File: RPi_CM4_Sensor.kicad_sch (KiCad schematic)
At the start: 16 parts, among them J1 RPi_pin, U1 SHT35, U2 SGP40, U3 APDS-9250, U4 SCD40

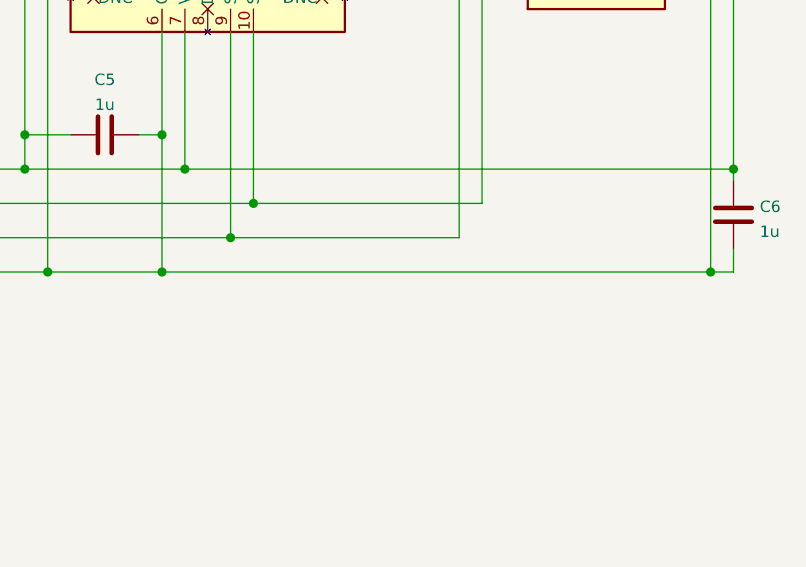
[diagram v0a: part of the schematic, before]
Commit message: feat: 温度センサを別基板に配置するためのピンヘッダを追加
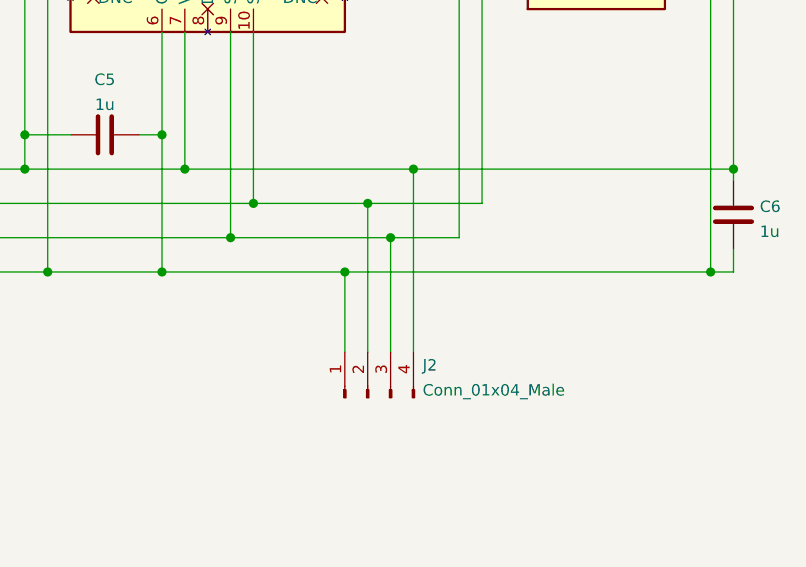
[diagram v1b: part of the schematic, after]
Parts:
- added J2: Conn_01x04_Male, Connector_PinHeader_2.54mm:PinHeader_1x04_P2.54mm_Vertical, symbol Connector:Conn_01x04_Male
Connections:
- net +3V3: now also J2.4 (Pin_4)
- net GND: now also J2.1 (Pin_1)
- net PIN_03: now also J2.2 (Pin_2)
- net PIN_05: now also J2.3 (Pin_3)
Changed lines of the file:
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@@
   (junction (at 209.55 88.9) (diameter 1.016) (color 0 0 0 0))
   (junction (at 212.09 85.09) (diameter 1.016) (color 0 0 0 0))
+  (junction (at 222.25 92.71) (diameter 1.016) (color 0 0 0 0))
+  (junction (at 224.79 85.09) (diameter 1.016) (color 0 0 0 0))
+  (junction (at 227.33 88.9) (diameter 1.016) (color 0 0 0 0))
+  (junction (at 229.87 81.28) (diameter 1.016) (color 0 0 0 0))
   (junction (at 262.89 92.71) (diameter 1.016) (color 0 0 0 0))
   (junction (at 265.43 81.28) (diameter 1.016) (color 0 0 0 0))
@@
     (stroke (width 0) (type solid) (color 0 0 0 0))
   )
-  (wire (pts (xy 201.93 92.71) (xy 262.89 92.71))
+  (wire (pts (xy 201.93 92.71) (xy 222.25 92.71))
     (stroke (width 0) (type solid) (color 0 0 0 0))
   )
@@
     (stroke (width 0) (type solid) (color 0 0 0 0))
   )
-  (wire (pts (xy 204.47 81.28) (xy 265.43 81.28))
+  (wire (pts (xy 204.47 81.28) (xy 229.87 81.28))
     (stroke (width 0) (type solid) (color 0 0 0 0))
   )
@@
     (stroke (width 0) (type solid) (color 0 0 0 0))
   )
-  (wire (pts (xy 209.55 88.9) (xy 234.95 88.9))
+  (wire (pts (xy 209.55 88.9) (xy 227.33 88.9))
     (stroke (width 0) (type solid) (color 0 0 0 0))
   )
@@
     (stroke (width 0) (type solid) (color 0 0 0 0))
   )
-  (wire (pts (xy 212.09 85.09) (xy 237.49 85.09))
+  (wire (pts (xy 212.09 85.09) (xy 224.79 85.09))
+    (stroke (width 0) (type solid) (color 0 0 0 0))
+  )
+  (wire (pts (xy 222.25 92.71) (xy 222.25 101.6))
+    (stroke (width 0) (type solid) (color 0 0 0 0))
+  )
+  (wire (pts (xy 222.25 92.71) (xy 262.89 92.71))
+    (stroke (width 0) (type solid) (color 0 0 0 0))
+  )
+  (wire (pts (xy 224.79 85.09) (xy 237.49 85.09))
+    (stroke (width 0) (type solid) (color 0 0 0 0))
+  )
+  (wire (pts (xy 224.79 101.6) (xy 224.79 85.09))
+    (stroke (width 0) (type solid) (color 0 0 0 0))
+  )
+  (wire (pts (xy 227.33 88.9) (xy 227.33 101.6))
+    (stroke (width 0) (type solid) (color 0 0 0 0))
+  )
+  (wire (pts (xy 227.33 88.9) (xy 234.95 88.9))
+    (stroke (width 0) (type solid) (color 0 0 0 0))
+  )
+  (wire (pts (xy 229.87 81.28) (xy 265.43 81.28))
+    (stroke (width 0) (type solid) (color 0 0 0 0))
+  )
+  (wire (pts (xy 229.87 101.6) (xy 229.87 81.28))
     (stroke (width 0) (type solid) (color 0 0 0 0))
   )
@@
     (pin "1")
     (pin "2")
+  )
+  (symbol (lib_id "Connector:Conn_01x04_Male") (at 224.79 106.68 90) (unit 1)
+    (in_bom yes) (on_board yes) (fields_autoplaced)
+    (property "Reference" "J2" (id 0) (at 230.8861 103.0791 90)
+      (effects (font (size 1.27 1.27)) (justify right))
+    )
+    (property "Value" "Conn_01x04_Male" (id 1) (at 230.8861 105.8542 90)
+      (effects (font (size 1.27 1.27)) (justify right))
+    )
+    (property "Footprint" "Connector_PinHeader_2.54mm:PinHeader_1x04_P2.54mm_Vertical" (id 2) (at 224.79 106.68 0)
+      (effects (font (size 1.27 1.27)) hide)
+    )
+    (property "Datasheet" "~" (id 3) (at 224.79 106.68 0)
+      (effects (font (size 1.27 1.27)) hide)
+    )
+    (pin "1")
+    (pin "2")
+    (pin "3")
+    (pin "4")
   )
   (symbol (lib_id "Sensor_Humidity:SHT30-DIS") (at 105.41 53.34 0) (unit 1)
@@
       (reference "J1") (unit 1) (value "RPi_pin") (footprint "Connector_PinHeader_2.54mm:PinHeader_2x20_P2.54mm_Vertical")
     )
+    (path "/b8c7c9f4-7e26-4126-b996-5566096740d9"
+      (reference "J2") (unit 1) (value "Conn_01x04_Male") (footprint "Connector_PinHeader_2.54mm:PinHeader_1x04_P2.54mm_Vertical")
+    )
     (path "/a7359116-bc92-46db-a3ba-fda3d67e12cb"
